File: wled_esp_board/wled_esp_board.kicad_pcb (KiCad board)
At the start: 2 copper layers, 35 x 35.5 mm, 26 parts, among them J1 Conn_01x09_Pin, J2 USB_C_Receptacle_USB2.0_16P, J3 Conn_01x09_Pin, J4 Conn_01x09_Pin, J5 Conn_01x09_Pin, SW1 Reset, SW2 Boot, U1 ESP32-S3-WROOM-1, U2 USBLC6-2SC6, U3 AP63203WU

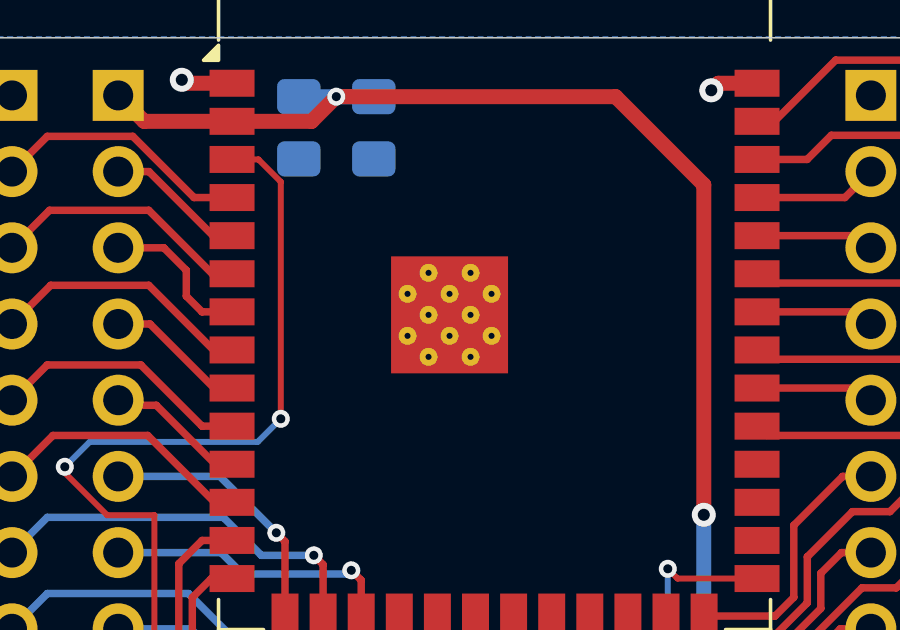
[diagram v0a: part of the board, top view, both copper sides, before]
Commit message: Update QR Code on base board
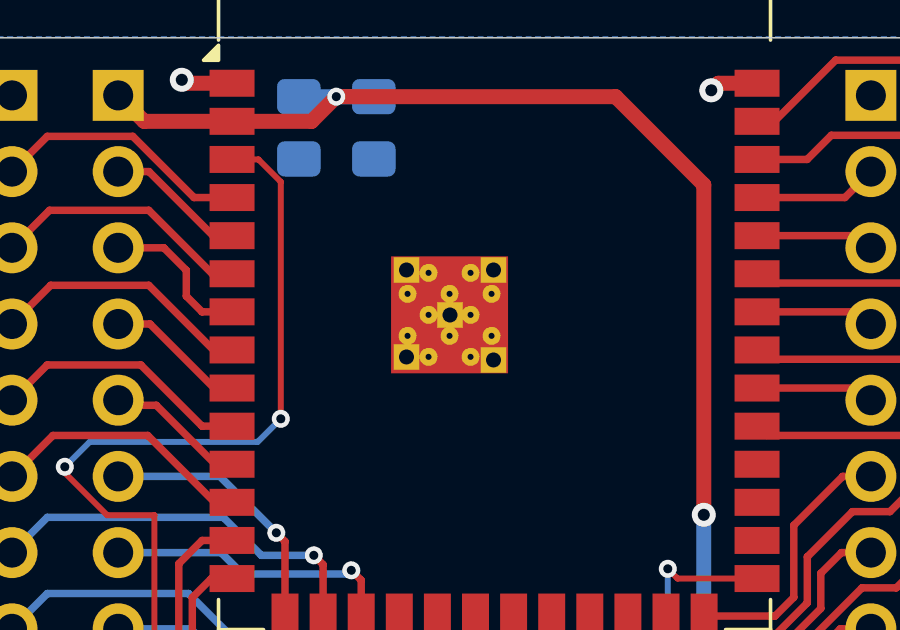
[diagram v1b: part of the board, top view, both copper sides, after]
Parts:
- added G***: LOGO, LOGO, B.Cu at (102.2, 72.8)
- added J10: Conn_01x01_Pin, Connector_PinHeader_1.00mm:PinHeader_1x01_P1.00mm_Horizontal, F.Cu at (101.5, 67.2)
- added J6: Conn_01x01_Pin, Connector_PinHeader_1.00mm:PinHeader_1x01_P1.00mm_Horizontal, F.Cu at (101.5, 64.2)
- added J7: Conn_01x01_Pin, Connector_PinHeader_1.00mm:PinHeader_1x01_P1.00mm_Horizontal, F.Cu at (98.6, 64.2)
- added J8: Conn_01x01_Pin, Connector_PinHeader_1.00mm:PinHeader_1x01_P1.00mm_Horizontal, F.Cu at (100.0, 65.7)
- added J9: Conn_01x01_Pin, Connector_PinHeader_1.00mm:PinHeader_1x01_P1.00mm_Horizontal, F.Cu at (98.6, 67.1)
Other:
- board text added: "DerNiccoo wled_esp_board v1"
